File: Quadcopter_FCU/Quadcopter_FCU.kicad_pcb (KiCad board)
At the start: 2 copper layers, 33 parts, among them J1 Conn_01x12_Male, J2 Conn_01x04_Male, J3 Conn_01x04_Male, J4 Conn_01x03_Male, J5 Conn_01x03_Male, J6 Conn_01x03_Male, J7 Conn_01x03_Male, J8 Conn_01x03_Male, J9 Conn_01x06_Male, SW1 SW_Push_Dual_x2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

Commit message: layed out ratsnest
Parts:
- moved J1 65.2 mm to (168.9, 130.8), turned to 270 degrees
- moved J5 57.0 mm to (180.3, 68.6)
- moved R5 47.6 mm to (139.7, 116.8)
- moved C9 39.0 mm to (150.8, 74.9), turned to 180 degrees
- moved J4 35.4 mm to (120.7, 73.7), turned to 180 degrees
- moved J3 35.1 mm to (134.6, 130.8), turned to 270 degrees
- moved J2 34.1 mm to (120.7, 100.3), turned to 180 degrees
- moved J6 33.8 mm to (180.3, 123.2)
- moved SW1 33.1 mm to (161.3, 87.6)
- moved R2 31.1 mm to (139.9, 111.8)
- moved J7 29.9 mm to (120.7, 127.0), turned to 180 degrees
- moved C11 27.0 mm to (161.6, 125.7)
- moved U3 27.0 mm to (149.9, 99.1)
- moved C10 25.8 mm to (161.6, 120.7)
- moved C8 25.7 mm to (155.3, 74.9)
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
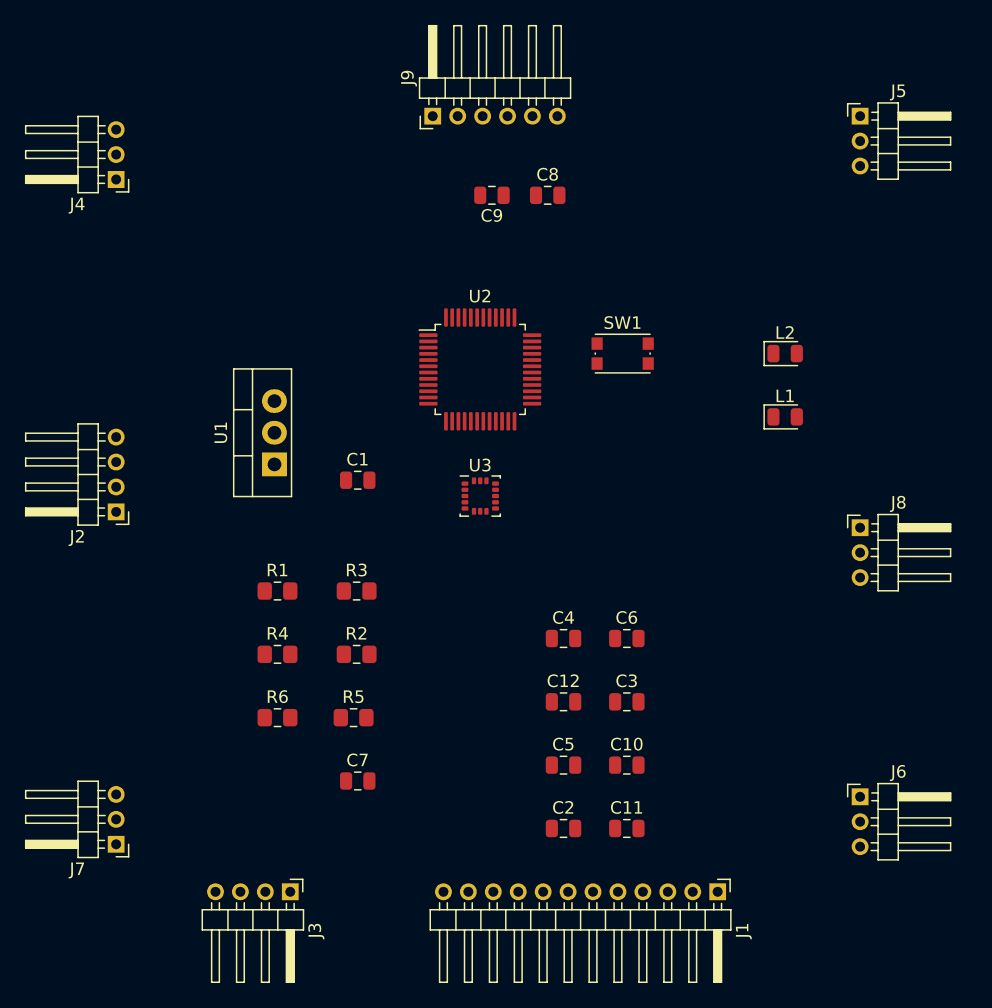
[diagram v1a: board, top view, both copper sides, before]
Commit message: finished initial routing for ground plane
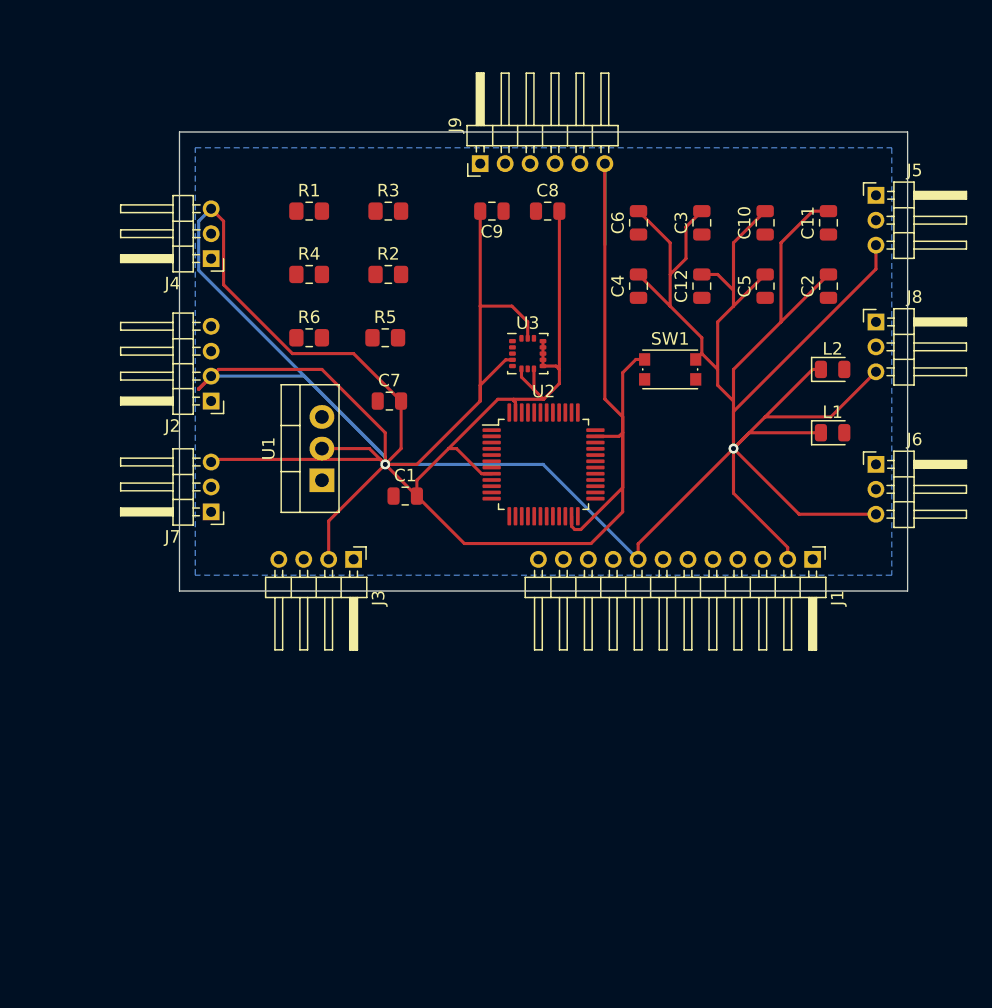
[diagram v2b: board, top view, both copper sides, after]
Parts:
- moved C11 51.2 mm to (177.8, 77.1), turned to 90 degrees
- moved C2 48.4 mm to (177.8, 82.2), turned to 90 degrees
- moved C10 44.9 mm to (172.7, 77.1), turned to 90 degrees
- moved C5 41.7 mm to (172.7, 82.2), turned to 90 degrees
- moved C3 38.9 mm to (167.6, 77.1), turned to 90 degrees
- moved C12 35.2 mm to (167.6, 82.2), turned to 90 degrees
- moved C6 33.4 mm to (162.6, 77.1), turned to 90 degrees
- moved R2 30.6 mm to (142.5, 81.3)
- moved R3 30.6 mm to (142.5, 76.2)
- moved R5 30.6 mm to (142.2, 86.4)
- moved C7 30.6 mm to (142.6, 91.4)
- moved R1 30.6 mm to (136.1, 76.2)
- moved R4 30.6 mm to (136.1, 81.3)
- moved R6 30.6 mm to (136.1, 86.4)
- moved C4 28.9 mm to (162.6, 82.2), turned to 90 degrees
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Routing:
- net GND: track 0.00 -> 468.3 mm, vias 0 -> 2
- added copper zone on B.Cu, net GND
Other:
- board outline added: 58.4 x 36.8 mm
- copper layers 2 -> 4
